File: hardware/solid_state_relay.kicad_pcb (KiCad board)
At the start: 2 copper layers, 19 x 33.4 mm, 22 parts, among them P1 CON-SENSOR2, P2 TST, P3 TST, P5 BOOT, Q1 2N7002P, U1 XMC1XXX24, U2 DRILL, U3 DRILL

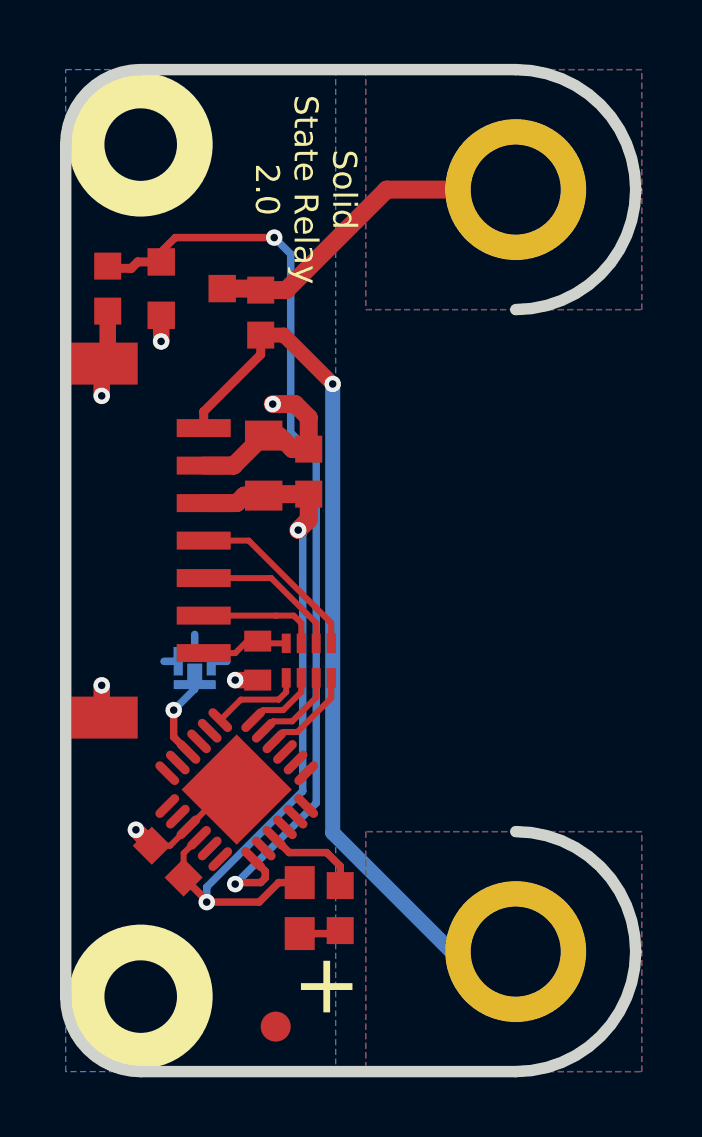
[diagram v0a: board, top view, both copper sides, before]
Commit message: Add "status" marking for status LED
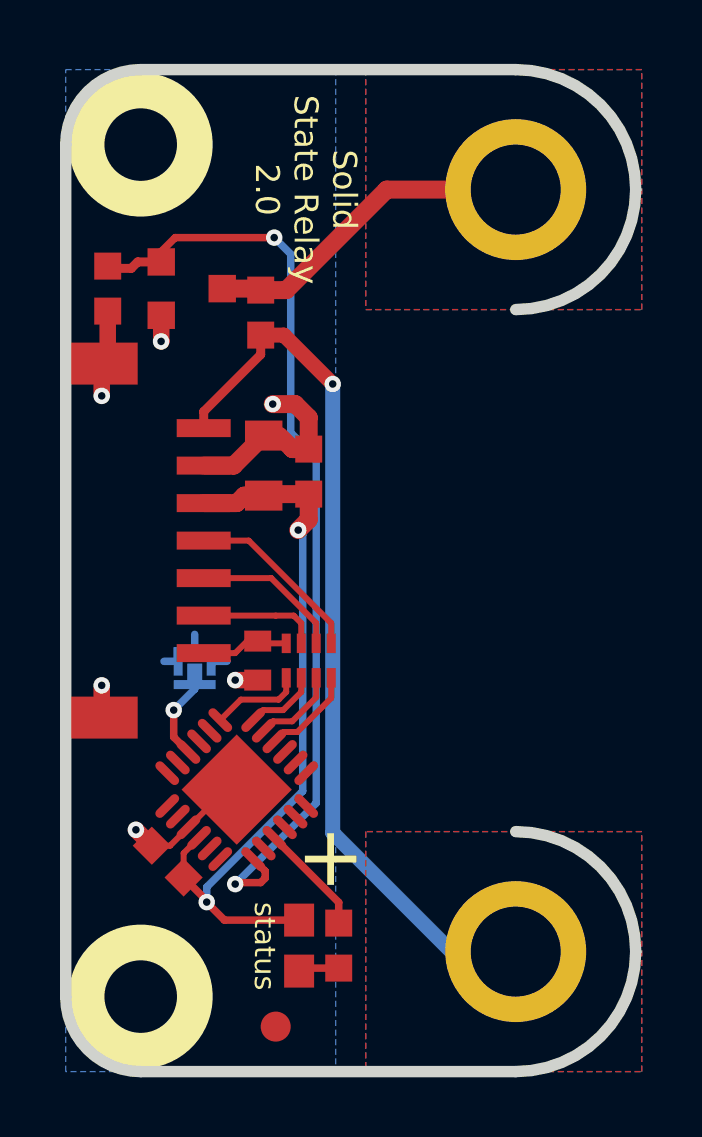
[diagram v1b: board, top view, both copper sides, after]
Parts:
- moved R3 1.25 mm to (107.5, 78.7)
- moved D1 1.25 mm to (106.2, 78.7)
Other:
- board text added: "status"
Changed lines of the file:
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@@
     (links 40)
     (no_connects 0)
-    (area 97.544999 48.644999 282.371482 165.089523)
+    (area 98.209499 49.309499 117.590501 83.090501)
     (thickness 1.6002)
-    (drawings 18)
-    (tracks 136)
+    (drawings 19)
+    (tracks 135)
     (zones 0)
     (modules 22)
@@
     (34 B.Paste user)
     (35 F.Paste user)
-    (36 B.SilkS user)
+    (36 B.SilkS user hide)
     (37 F.SilkS user)
     (38 B.Mask user)
@@
   )
   (setup
-    (last_trace_width 0.59944)
+    (last_trace_width 0.25)
     (user_trace_width 0.25)
     (user_trace_width 0.29972)
@@
   )
   (module kicad-libraries:D0603E (layer Vorderseite)
-    (at 106.2 77.45 270)
+    (at 106.18 78.7 270)
     (attr smd)
     (fp_text reference D1 (at 0.85 0.45 270) (layer F.Fab)
@@
   )
   (module kicad-libraries:R0603F (layer Vorderseite)
-    (at 107.55 77.45 270)
+    (at 107.5 78.7 270)
     (attr smd)
     (fp_text reference R3 (at 0.05 0.225 270) (layer F.Fab)
@@
       (xy 2.3114 -1.41732) (xy 2.3114 -1.67132) (xy 2.3114 -1.67132)) (layer B.SilkS) (width 0.00254))
   )
+  (gr_text status (at 105.03 78.72 270) (layer F.SilkS)
+    (effects (font (size 0.7 0.7) (thickness 0.15)))
+  )
   (gr_line (start 113.4 74.9) (end 108.9 74.9) (angle 90) (layer F.Fab) (width 0.381))
   (gr_line (start 107.9 58.5) (end 107.9 73.9) (angle 90) (layer F.Fab) (width 0.381))
@@
   (gr_arc (start 108.9 58.5) (end 107.9 58.5) (angle 90) (layer F.Fab) (width 0.381))
   (gr_arc (start 108.9 73.9) (end 108.9 74.9) (angle 90) (layer F.Fab) (width 0.381))
-  (gr_text + (at 107.1 80) (layer F.SilkS)
+  (gr_text + (at 107.23 75.75) (layer F.SilkS)
     (effects (font (size 2 2) (thickness 0.3)))
   )
@@
   (segment (start 102.491332 74.758668) (end 101.88033 75.36967) (width 0.2) (layer Vorderseite) (net 2))
   (segment (start 101.88033 75.36967) (end 101.26967 75.36967) (width 0.2) (layer Vorderseite) (net 2))
+  (segment (start 103.1 77.25) (end 103.1 77.26) (width 0.25) (layer Vorderseite) (net 3))
+  (segment (start 103.6899 77.8499) (end 106.18 77.8499) (width 0.25) (layer Vorderseite) (net 3) (status 800000))
+  (segment (start 103.1 77.26) (end 103.6899 77.8499) (width 0.25) (layer Vorderseite) (net 3))
   (segment (start 106.5 63.65) (end 106.5 64.5) (width 0.59944) (layer Vorderseite) (net 3))
   (segment (start 103.125 77.225) (end 103.15 77.25) (width 0.25) (layer Vorderseite) (net 3))
@@
   (via (at 106.15 64.85) (size 0.55) (drill 0.25) (layers Vorderseite Rückseite) (net 3))
   (segment (start 106.5 64.5) (end 106.15 64.85) (width 0.59944) (layer Vorderseite) (net 3))
-  (segment (start 106.2 76.5999) (end 105.5001 76.5999) (width 0.25) (layer Vorderseite) (net 3))
-  (segment (start 105.5001 76.5999) (end 104.85 77.25) (width 0.25) (layer Vorderseite) (net 3))
-  (segment (start 104.85 77.25) (end 103.15 77.25) (width 0.25) (layer Vorderseite) (net 3))
   (segment (start 103.15 77.25) (end 102.33033 76.43033) (width 0.25) (layer Vorderseite) (net 3))
   (segment (start 102.33033 76.83033) (end 102.33033 76.43033) (width 0.2) (layer Vorderseite) (net 3))
@@
   (segment (start 105.7507 68.625) (end 104.875 68.625) (width 0.2) (layer Vorderseite) (net 9))
   (segment (start 104.875 68.625) (end 104.8 68.55) (width 0.2) (layer Vorderseite) (net 9))
-  (segment (start 106.2 78.3001) (end 107.4499 78.3001) (width 0.25) (layer Vorderseite) (net 10))
-  (segment (start 107.4499 78.3001) (end 107.55 78.2) (width 0.25) (layer Vorderseite) (net 10))
+  (segment (start 107.5 79.45) (end 106.2801 79.45) (width 0.25) (layer Vorderseite) (net 10) (status C00000))
+  (segment (start 106.2801 79.45) (end 106.18 79.5501) (width 0.2) (layer Vorderseite) (net 10) (status C00000))
   (segment (start 102.7 70) (end 102.7 69.6) (width 0.25) (layer Rückseite) (net 11))
   (segment (start 102.491332 72.244885) (end 102.491332 72.241332) (width 0.25) (layer Vorderseite) (net 11))
@@
   (segment (start 100.8 55.911) (end 101.584 55.911) (width 0.29972) (layer Vorderseite) (net 12))
   (segment (start 100.586 56.125) (end 100.8 55.911) (width 0.29972) (layer Vorderseite) (net 12))
+  (segment (start 105.355115 75.108668) (end 105.355115 75.115115) (width 0.2) (layer Vorderseite) (net 13) (status C00000))
+  (segment (start 105.355115 75.115115) (end 107.5 77.26) (width 0.25) (layer Vorderseite) (net 13) (status 400000))
+  (segment (start 107.5 77.26) (end 107.5 77.95) (width 0.25) (layer Vorderseite) (net 13) (status 800000))
   (segment (start 105.355115 75.108668) (end 105.358668 75.108668) (width 0.25) (layer Vorderseite) (net 13))
-  (segment (start 105.358668 75.108668) (end 105.85 75.6) (width 0.25) (layer Vorderseite) (net 13))
-  (segment (start 105.85 75.6) (end 107.1 75.6) (width 0.25) (layer Vorderseite) (net 13))
-  (segment (start 107.1 75.6) (end 107.55 76.05) (width 0.25) (layer Vorderseite) (net 13))
-  (segment (start 107.55 76.05) (end 107.55 76.7) (width 0.25) (layer Vorderseite) (net 13))
   (segment (start 103.551992 71.184225) (end 104.236217 70.5) (width 0.2) (layer Vorderseite) (net 14))
   (segment (start 105.7507 70.2493) (end 105.7507 69.775) (width 0.2) (layer Vorderseite) (net 14))

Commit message: fix outline edge cuts layer, fix weee logo
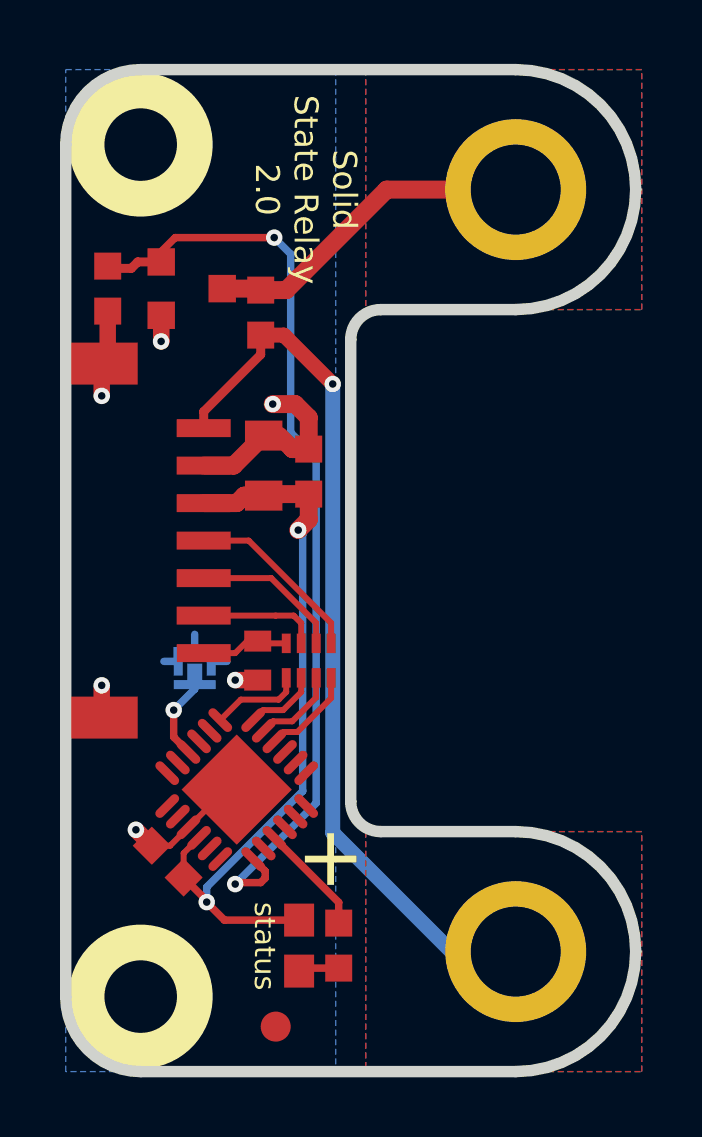
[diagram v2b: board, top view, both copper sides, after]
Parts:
- VAL: footprint WEEE_7mm -> kicad-libraries:WEEE_7mm
- moved VAL 0.80 mm to (102.9, 58.5), turned to 90 degrees
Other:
- outline, holes or cut-outs redrawn

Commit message: change led position
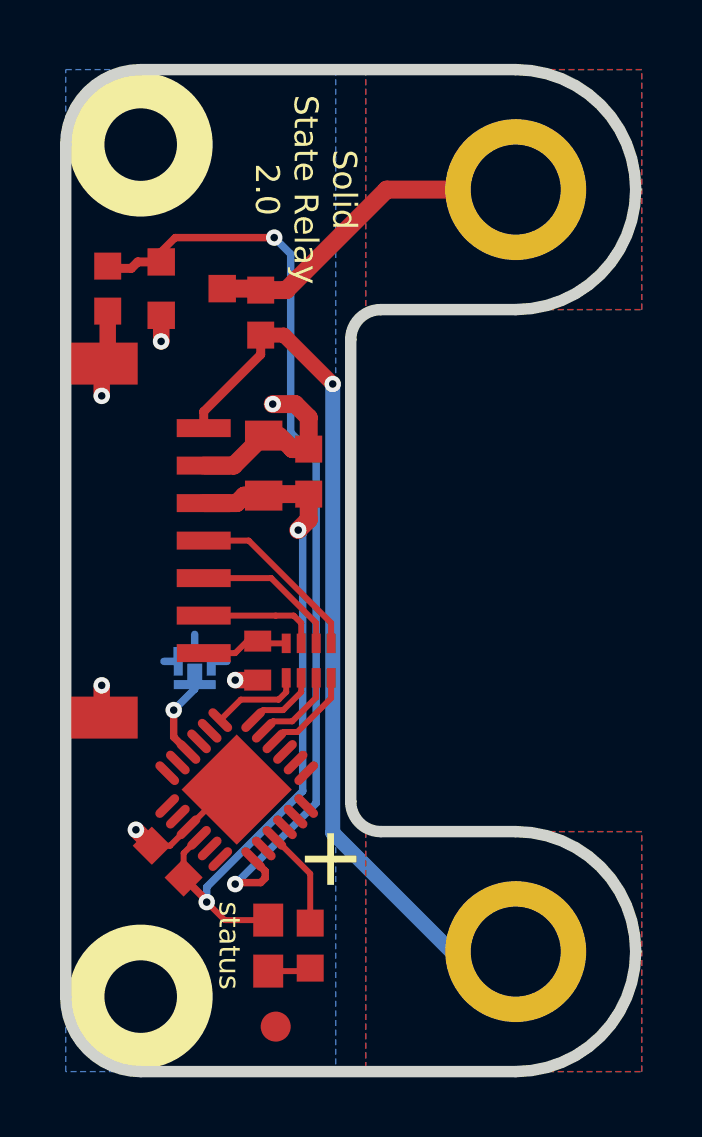
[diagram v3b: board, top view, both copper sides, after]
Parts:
- moved D1 1.03 mm to (105.2, 78.7)
- moved R3 0.95 mm to (106.5, 78.7)
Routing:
- net VCC: track 25.3 -> 24.2 mm
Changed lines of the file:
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@@
   )
   (layers
-    (0 Vorderseite mixed hide)
+    (0 Vorderseite mixed)
     (31 Rückseite signal hide)
     (32 B.Adhes user)
@@
     (pad_to_mask_clearance 0)
     (aux_axis_origin 0 0)
-    (visible_elements FFFFBFBF)
+    (visible_elements FFFF7FBF)
     (pcbplotparams
       (layerselection 0x00008_00000000)
@@
   )
   (module kicad-libraries:D0603E (layer Vorderseite)
-    (at 106.18 78.7 270)
+    (at 105.15 78.7 270)
     (attr smd)
     (fp_text reference D1 (at 0.85 0.45 270) (layer F.Fab)
@@
   )
   (module kicad-libraries:R0603F (layer Vorderseite)
-    (at 107.5 78.7 270)
+    (at 106.55 78.7 270)
     (attr smd)
     (fp_text reference R3 (at 0.05 0.225 270) (layer F.Fab)
@@
       (xy 2.3114 -1.41732) (xy 2.3114 -1.67132) (xy 2.3114 -1.67132)) (layer B.SilkS) (width 0.00254))
   )
-  (gr_text status (at 105.03 78.72 270) (layer F.SilkS)
+  (gr_text status (at 103.85 78.7 270) (layer F.SilkS)
     (effects (font (size 0.7 0.7) (thickness 0.15)))
   )
@@
   (segment (start 102.491332 74.758668) (end 101.88033 75.36967) (width 0.2) (layer Vorderseite) (net 2))
   (segment (start 101.88033 75.36967) (end 101.26967 75.36967) (width 0.2) (layer Vorderseite) (net 2))
-  (segment (start 103.1 77.25) (end 103.1 77.26) (width 0.25) (layer Vorderseite) (net 3))
-  (segment (start 103.6899 77.8499) (end 106.18 77.8499) (width 0.25) (layer Vorderseite) (net 3))
-  (segment (start 103.1 77.26) (end 103.6899 77.8499) (width 0.25) (layer Vorderseite) (net 3))
+  (segment (start 105.15 77.8499) (end 103.6999 77.8499) (width 0.2) (layer Vorderseite) (net 3))
+  (segment (start 103.6999 77.8499) (end 103.1 77.25) (width 0.2) (layer Vorderseite) (net 3))
   (segment (start 106.5 63.65) (end 106.5 64.5) (width 0.59944) (layer Vorderseite) (net 3))
   (segment (start 103.125 77.225) (end 103.15 77.25) (width 0.25) (layer Vorderseite) (net 3))
@@
   (segment (start 105.7507 68.625) (end 104.875 68.625) (width 0.2) (layer Vorderseite) (net 9))
   (segment (start 104.875 68.625) (end 104.8 68.55) (width 0.2) (layer Vorderseite) (net 9))
-  (segment (start 107.5 79.45) (end 106.2801 79.45) (width 0.25) (layer Vorderseite) (net 10))
+  (segment (start 106.55 79.45) (end 106.4499 79.5501) (width 0.2) (layer Vorderseite) (net 10))
+  (segment (start 106.4499 79.5501) (end 105.15 79.5501) (width 0.2) (layer Vorderseite) (net 10))
   (segment (start 106.2801 79.45) (end 106.18 79.5501) (width 0.2) (layer Vorderseite) (net 10))
   (segment (start 102.7 70) (end 102.7 69.6) (width 0.25) (layer Rückseite) (net 11))
@@
   (segment (start 100.8 55.911) (end 101.584 55.911) (width 0.29972) (layer Vorderseite) (net 12))
   (segment (start 100.586 56.125) (end 100.8 55.911) (width 0.29972) (layer Vorderseite) (net 12))
+  (segment (start 105.355115 75.108668) (end 106.55 76.303553) (width 0.2) (layer Vorderseite) (net 13))
+  (segment (start 106.55 76.303553) (end 106.55 77.95) (width 0.2) (layer Vorderseite) (net 13))
   (segment (start 105.355115 75.108668) (end 105.355115 75.115115) (width 0.2) (layer Vorderseite) (net 13))
-  (segment (start 105.355115 75.115115) (end 107.5 77.26) (width 0.25) (layer Vorderseite) (net 13))
-  (segment (start 107.5 77.26) (end 107.5 77.95) (width 0.25) (layer Vorderseite) (net 13))
   (segment (start 105.355115 75.108668) (end 105.358668 75.108668) (width 0.25) (layer Vorderseite) (net 13))
   (segment (start 103.551992 71.184225) (end 104.236217 70.5) (width 0.2) (layer Vorderseite) (net 14))
@@
     (polygon
       (pts
-        (xy 107.4 82.9) (xy 98.4 82.9) (xy 98.4 49.5) (xy 107.4 49.5) (xy 107.4 82.9)
+        (xy 107.4 82.9) (xy 98.4 82.9) (xy 98.4 49.5) (xy 107.4 49.5)
       )
     )

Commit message: specify processor type
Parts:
- U1: value XMC1XXX24 -> XMC110024
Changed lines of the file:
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@@
       (effects (font (size 0.3 0.3) (thickness 0.075)))
     )
-    (fp_text value XMC1XXX24 (at 0 0.8 315) (layer F.Fab)
+    (fp_text value XMC110024 (at 0 0.8 315) (layer F.Fab)
       (effects (font (size 0.3 0.3) (thickness 0.075)))
     )
